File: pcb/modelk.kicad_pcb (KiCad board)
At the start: 2 copper layers, 150 x 38 mm, 50 parts, among them J1 JST-PH connector, J2 Conn_01x20, J3 User exposed, J4 Conn_01x12, J5 Conn_01x04, J6 Conn_01x08, J7 Faston PCB mount, J8 Dupont for power profiling, SW1 SW_reset, U1 nice_nano, U2 74HC595, U3 74HC595, U4 74HC595

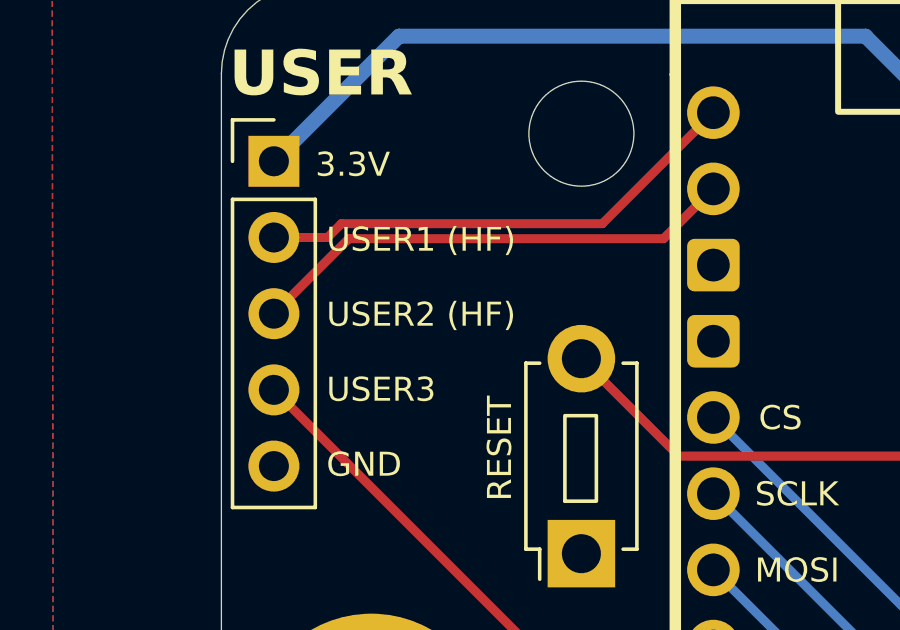
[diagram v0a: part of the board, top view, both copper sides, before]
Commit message: Modified user text to be the actual pin
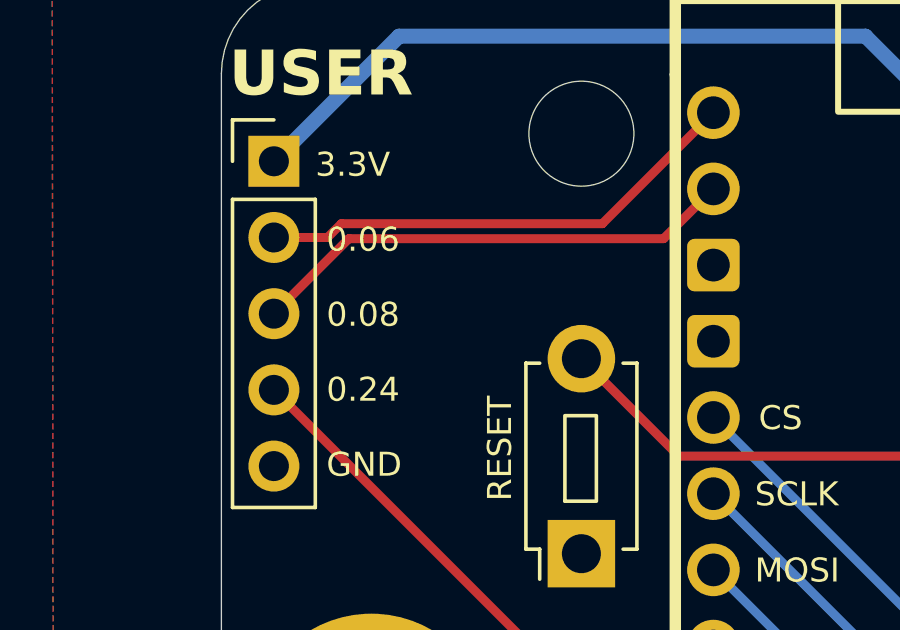
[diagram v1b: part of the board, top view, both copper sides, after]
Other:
- board text added: "0.06"
- board text added: "0.08"
- board text added: "0.24"
- board text removed: "USER1 (HF)"
- board text removed: "USER2 (HF)"
- board text removed: "USER3"

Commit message: Labels
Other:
- board text added: "ONLY COMPATIBLE WITH NICE!NANO DUE TO SPI"
- board text removed: "only compatible with nice!nano due to SPI"

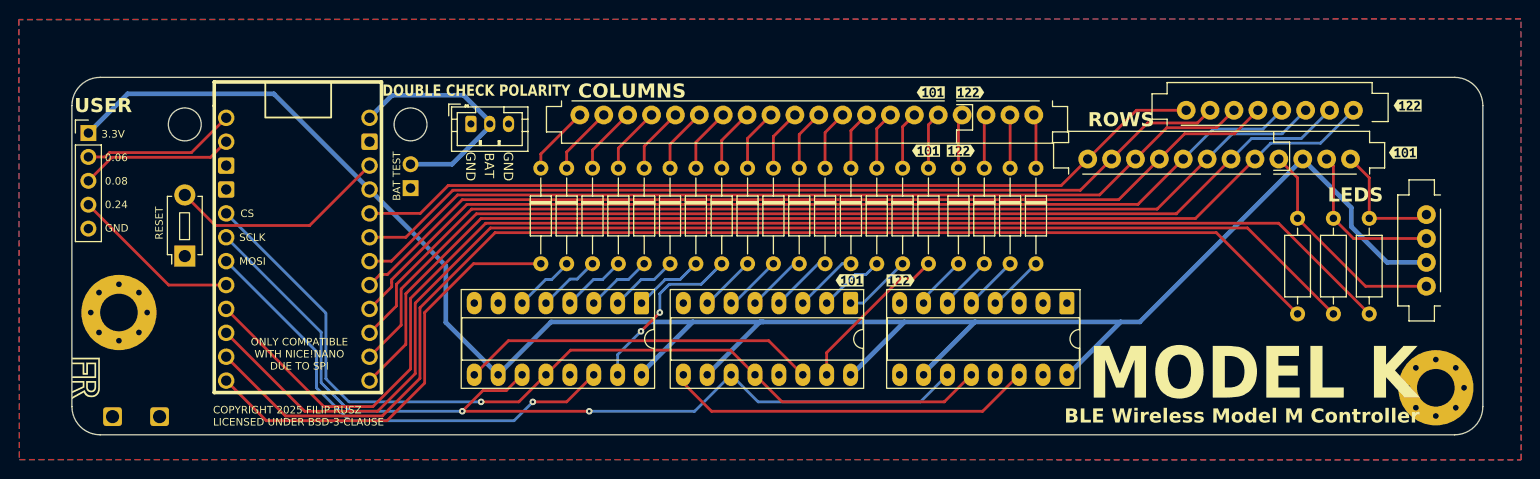
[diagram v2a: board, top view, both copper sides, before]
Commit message: Added pictograms
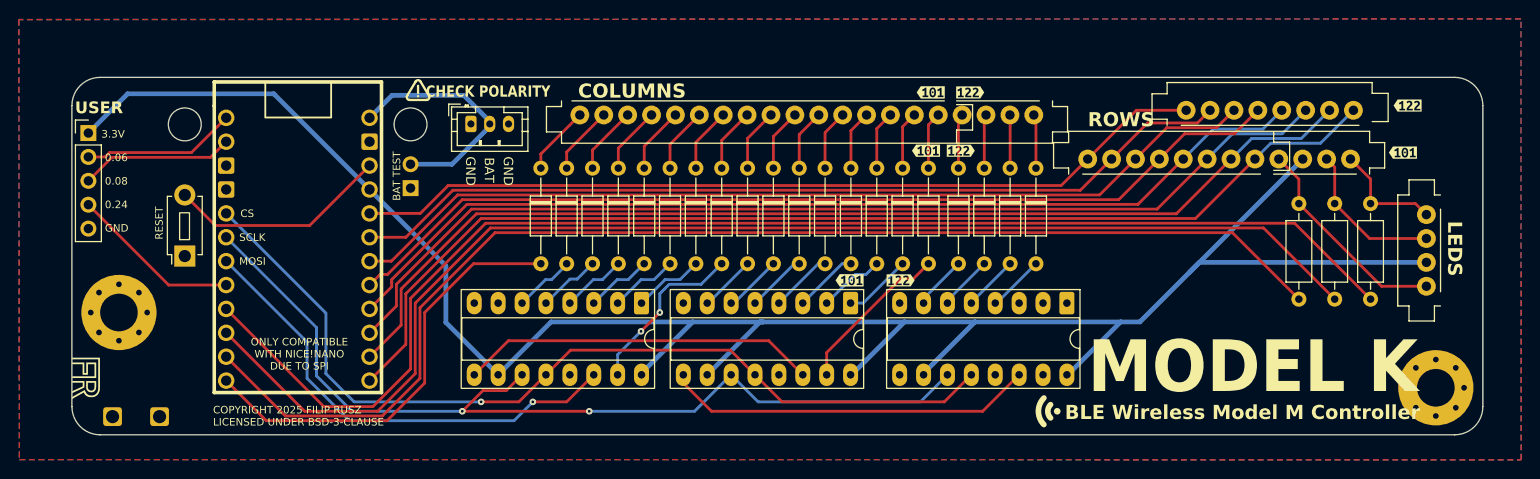
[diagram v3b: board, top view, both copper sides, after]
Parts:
- added REF**: LOGO-wireless, Library:LOGO-wireless, F.Cu at (169.5, 82.5)
- added REF**: LOGO-warning, Library:LOGO-warning, F.Cu at (101.6, 48.4)
- moved G*** 79.1 mm to (186.5, 68.0)
- moved R1 1.57 mm to (195.2, 60.4)
- moved R2 1.57 mm to (199.0, 60.4)
- moved R3 1.57 mm to (202.8, 60.4)
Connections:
- net led0r renamed Net-(J4-Pin_12)
- net led1r renamed Net-(J4-Pin_11)
- net led2r renamed Net-(J4-Pin_9)
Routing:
- net +3.3V: track 215.0 -> 221.8 mm
- net Net-(J4-Pin_9): track 23.8 -> 22.8 mm
- net Net-(J4-Pin_11): track 17.4 -> 16.4 mm
- net Net-(J4-Pin_12): track 13.4 -> 12.6 mm
- net led1: track 137.4 -> 136.9 mm
- net led0: track 132.6 -> 132.0 mm
- net led2: track 142.3 -> 141.8 mm
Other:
- board text added: "CHECK POLARITY"
- board text added: "ORDER NUMBER"
- board text removed: "DOUBLE CHECK POLARITY"

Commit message: Fixed connector position
Also added Designed In CZ text on silkscreen and distributed traces in
the middle.
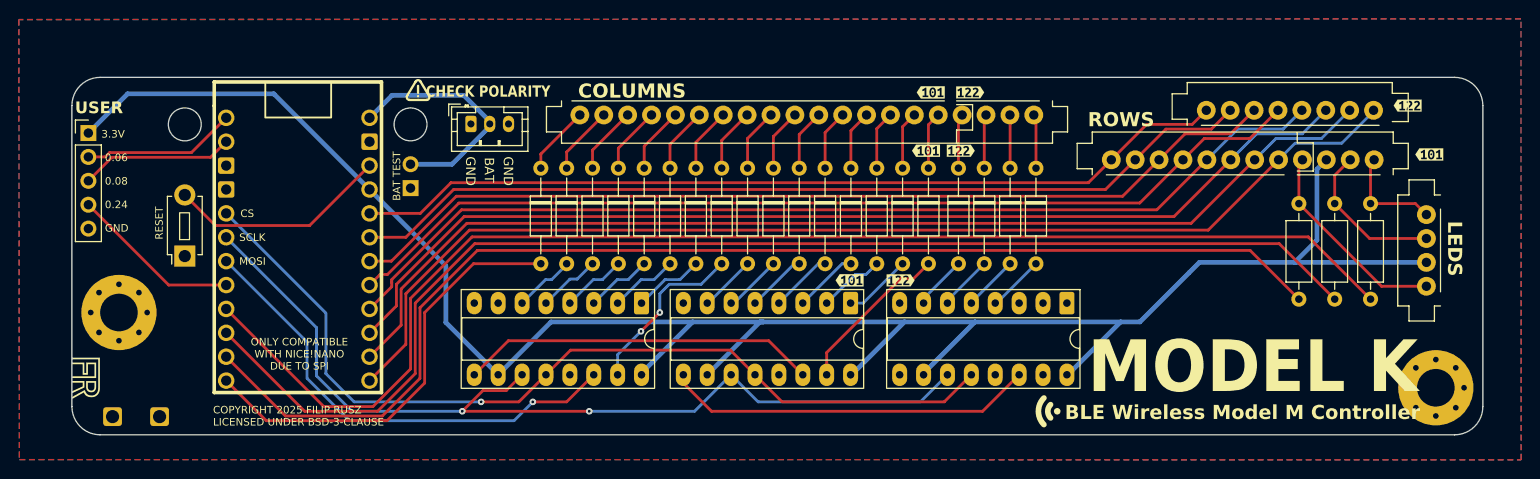
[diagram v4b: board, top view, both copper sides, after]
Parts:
- moved kibuzzard-684FF45F 2.81 mm to (209.1, 55.2)
- moved J4 2.51 mm to (189.2, 54.8)
- moved J6 2.14 mm to (194.3, 49.1)
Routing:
- net +3.3V: track 221.8 -> 217.0 mm
- net /row2: track 98.5 -> 100.8 mm
- net /row5: track 110.7 -> 112.8 mm
- net /row6: track 115.2 -> 117.3 mm
- net /row4: track 106.2 -> 108.3 mm
- net /row3: track 102.1 -> 104.3 mm
- net /row1: track 95.0 -> 97.1 mm
- net /row0: track 91.4 -> 93.5 mm
- net /row7: track 119.7 -> 121.4 mm
- net led0: track 132.0 -> 130.5 mm
- net led1: track 136.9 -> 135.5 mm
- net led2: track 141.8 -> 140.6 mm
- net Net-(J4-Pin_9): track 22.8 -> 22.0 mm
- net Net-(J4-Pin_12): track 12.6 -> 11.8 mm
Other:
- board text added: "DESIGNED IN THE CZECH REPUBLIC MANUFACTURED IN CHINA"
- board text removed: "TODO: Better font?"
